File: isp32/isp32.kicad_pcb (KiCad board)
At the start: 2 copper layers, 55.5 x 48.5 mm, 101 parts, among them J1 BAT1, J10 LoRa_ANT, J2 Switching, J3 USB_C_Receptacle_USB2.0, J4 ESP_JTAG, J5 GPS_ANT, J6 F0, J7 F1, J8 Flash_SPI, J9 ANT, M1 Motor_Servo, M2 Motor_Servo, M3 Motor_Servo, M4 Motor_Servo, Q1 BSS138, Q2 BSS138, Q3 IRLML6402, Q4 BSS138, Q5 IRLML6402, Q6 S8050, Q7 S8050, Q8 S8050, SW1 RST, SW2 IO0, U10 BMP280, U11 MPU-9250, U12 CH340C, U2 USBLC6-2SC6, U3 ESP32-WROOM-32U, U4 AMS1117-3.3, U5 MP2303ADN, U7 NEO-XM, U8 AT25SF081-SSHD-X, U9 RFM98W-315S2

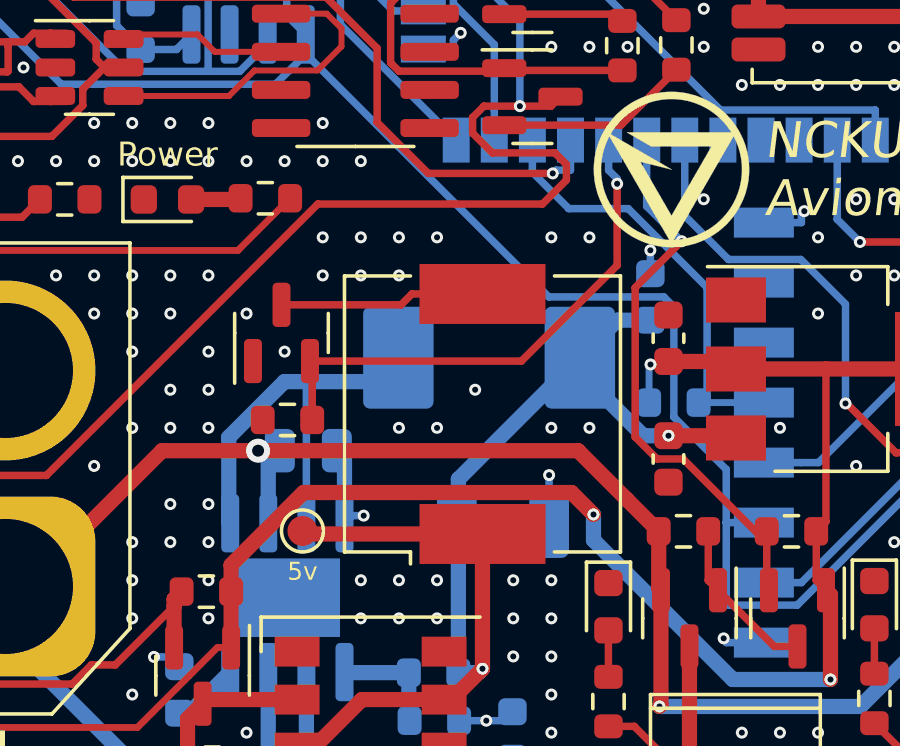
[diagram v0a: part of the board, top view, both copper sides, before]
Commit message: Change buzzer type
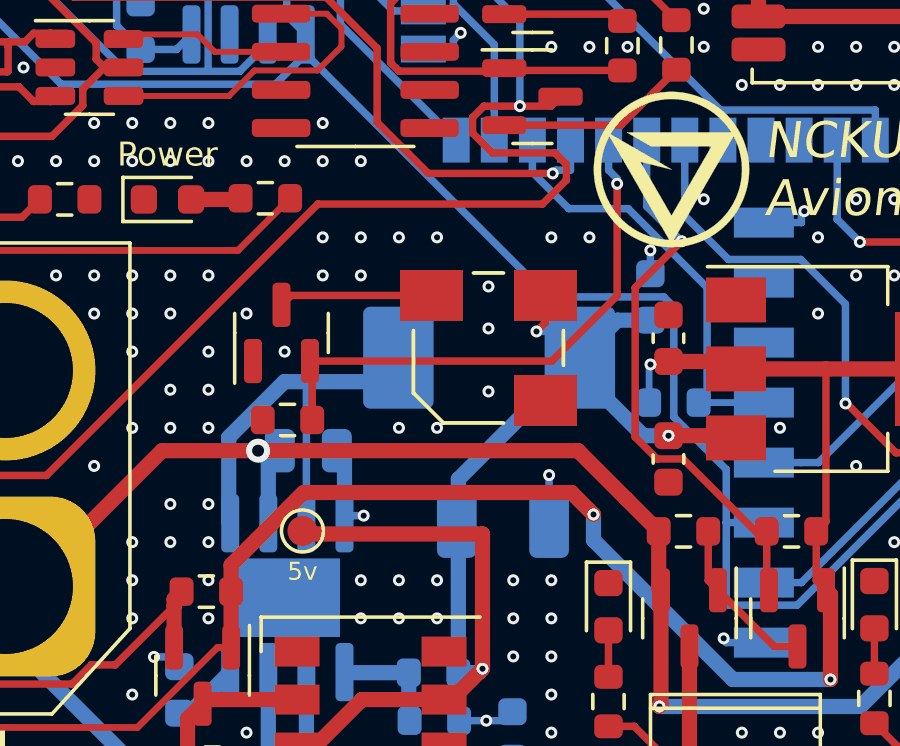
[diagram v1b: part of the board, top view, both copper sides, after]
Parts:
- removed BZ1: Buzzer, Buzzer_Beeper:Buzzer_CUI_CPT-9019S-SMT
- added LS1: 5020, Buzzer:XDCR_KSSG33J12-3, F.Cu at (83.9, 69.5)
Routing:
- net +5V: track 154.7 -> 157.8 mm, vias 6 -> 7
- net Net-(LS1-PadN): track 6.85 -> 5.13 mm
- net Buzz: track 17.8 -> 18.4 mm
- net GND: vias 465 -> 464

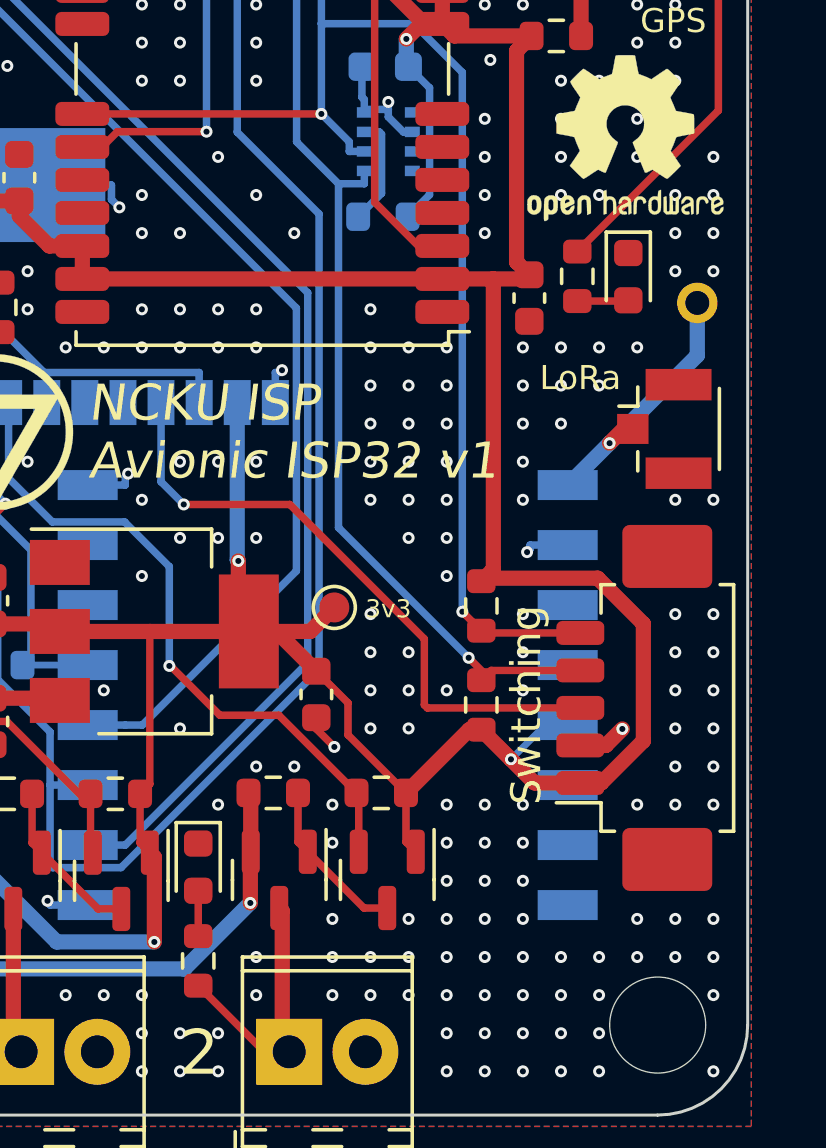
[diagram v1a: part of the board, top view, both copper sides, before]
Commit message: Switching port flip
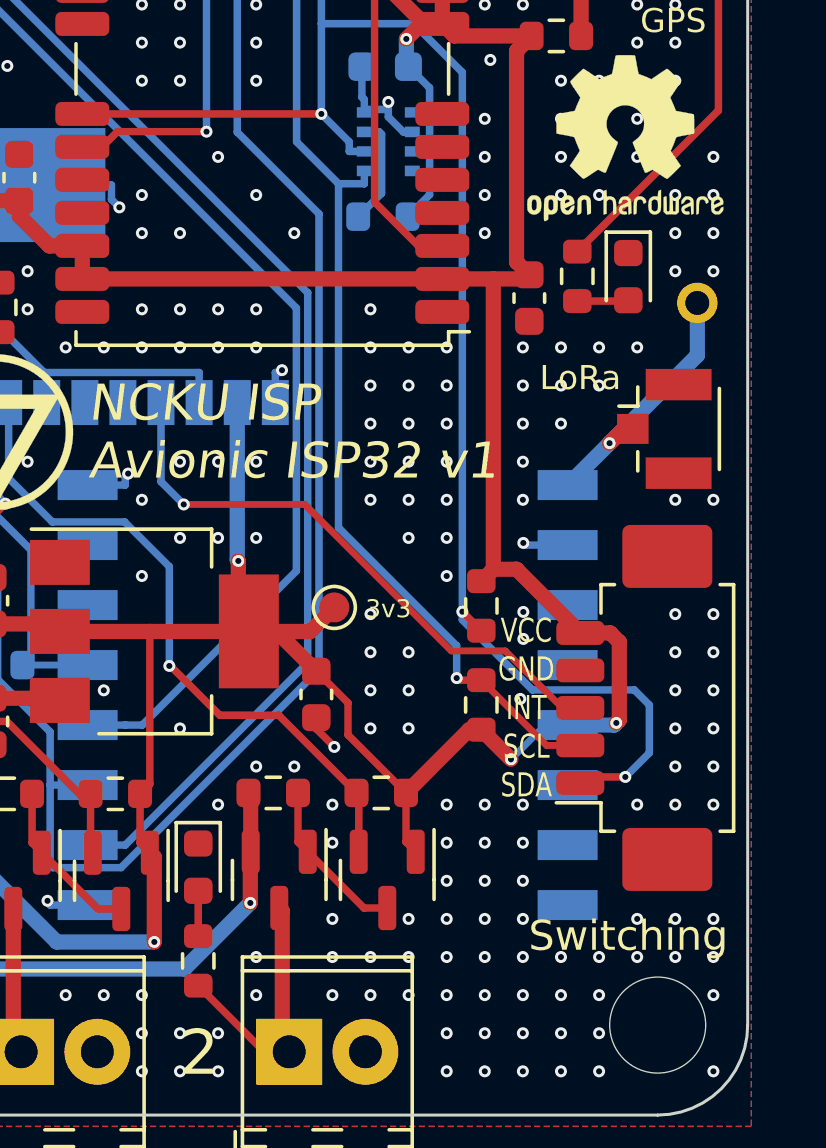
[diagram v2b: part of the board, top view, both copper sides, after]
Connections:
- J2 pad 1: +3V3 -> SDA
- J2 pad 2: GND -> SCL
- J2 pad 4: SCL -> GND
- J2 pad 5: SDA -> +3V3
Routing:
- net SDA: track 56.4 -> 65.0 mm, vias 2 -> 3
- net +3V3: track 260.9 -> 255.4 mm, vias 6 -> 7
- net GND: track 50.1 -> 48.4 mm, vias 464 -> 462
- net SCL: track 52.0 -> 53.3 mm
- net EXT_INT: track 21.0 -> 19.7 mm
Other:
- board text added: "VCC GND INT SCL SDA"

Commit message: Add water mark
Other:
- board text added: "JLCJLCJLCJLC"
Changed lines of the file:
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@@
     (effects (font (size 0.8 0.8) (thickness 0.15)))
   )
-  (gr_text "VCC\nGND\nINT\nSCL\nSDA" (at 107.7 72.7) (layer "F.SilkS")
-    (effects (font (size 0.8 0.6) (thickness 0.1)))
+  (gr_text "VCC\nGND\nINT\nSCL\nSDA" (at 107.7 72.8) (layer "F.SilkS")
+    (effects (font (size 0.8 0.6) (thickness 0.15)))
   )
   (gr_text "LoRa" (at 109.5 61.7) (layer "F.SilkS")
     (effects (font (size 0.8 0.8) (thickness 0.15)))
   )
+  (gr_text "JLCJLCJLCJLC" (at 98.9 52.9 90) (layer "F.SilkS")
+    (effects (font (size 1 1) (thickness 0.15)))
+  )
   (gr_text "3V3 TDI TCK TMS TDO GND" (at 74.1 46.4) (layer "F.SilkS")

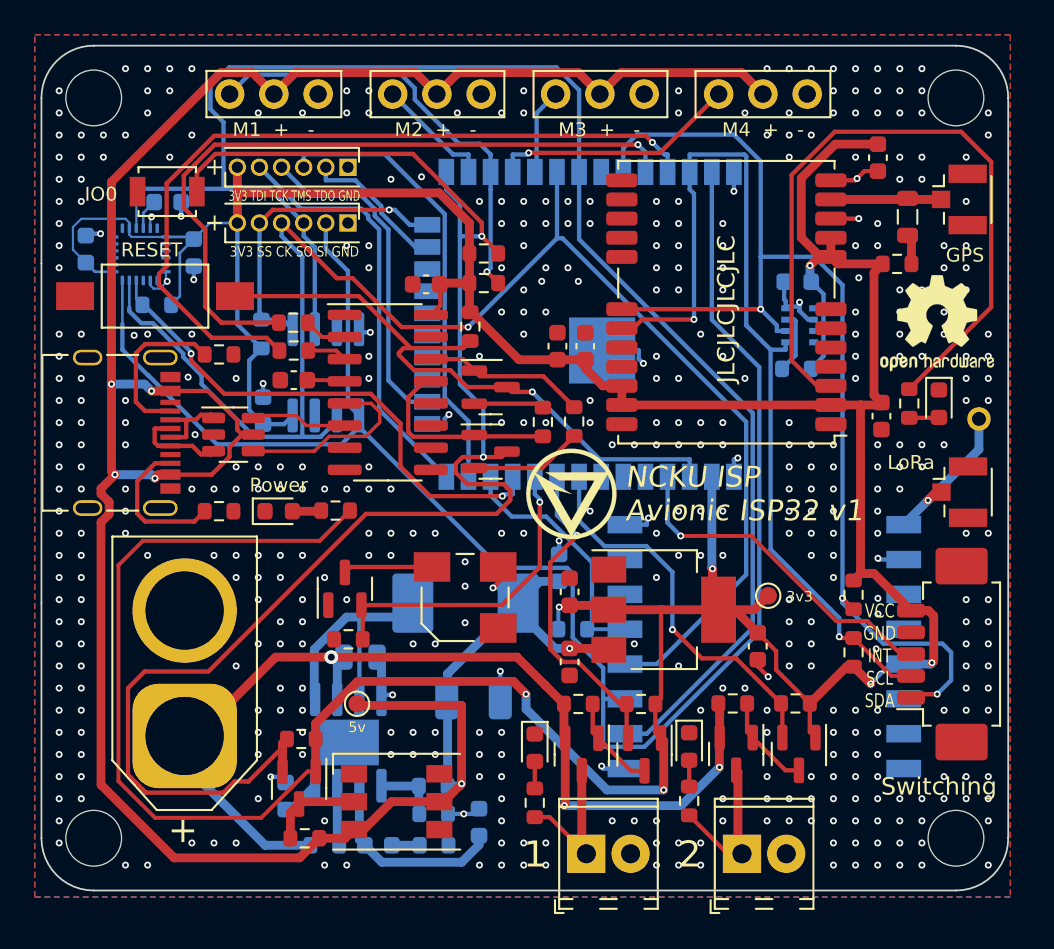
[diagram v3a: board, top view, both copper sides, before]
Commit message: Add sd card and pwm controller
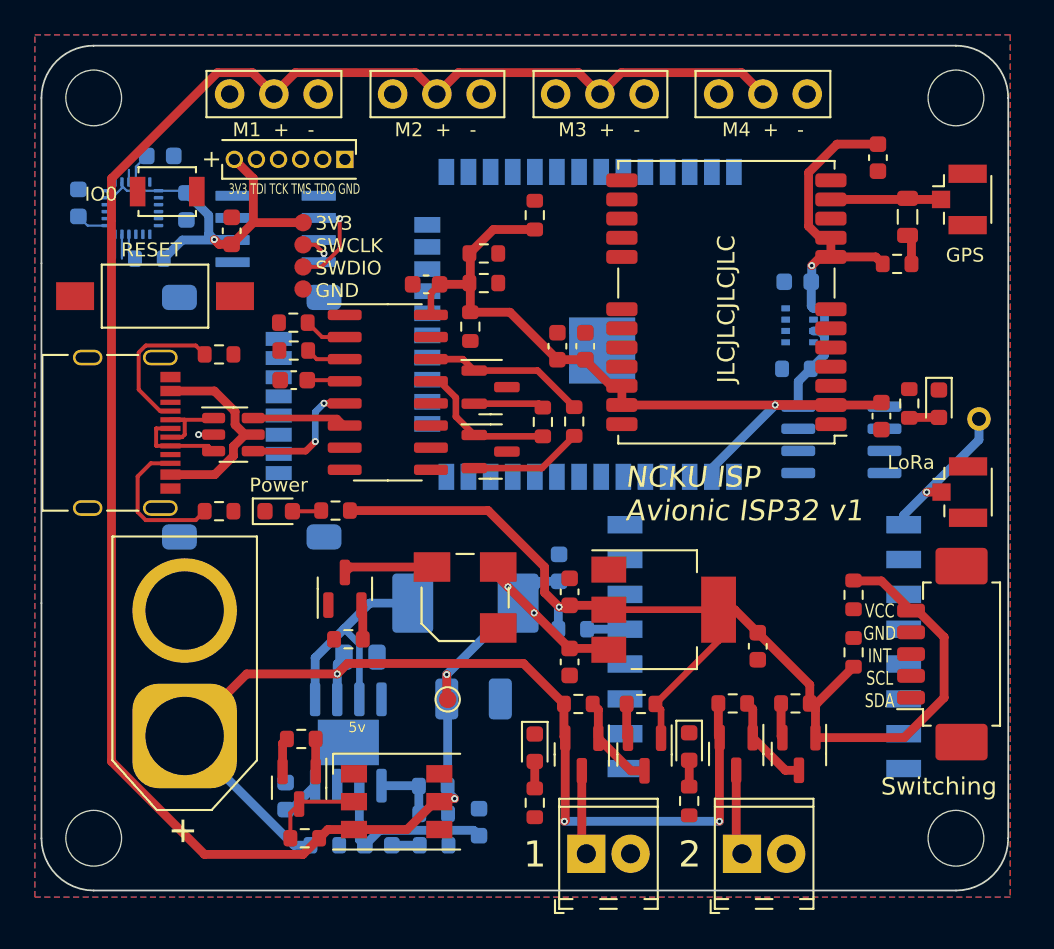
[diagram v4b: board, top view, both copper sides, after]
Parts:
- removed C20: 100n, Capacitor_SMD:C_0603_1608Metric
- removed G***: LOGO, isp_logo:isp_logo
- removed J8: Flash_SPI, Connector_PinHeader_1.27mm:PinHeader_1x06_P1.27mm_Vertical
- removed REF**: OSHW-Logo2_7.3x6mm_SilkScreen, Symbol:OSHW-Logo2_7.3x6mm_SilkScreen
- removed U8: AT25SF081-SSHD-X, Package_SO:SOIC-8_3.9x4.9mm_P1.27mm
- added C3: 100n, Capacitor_SMD:C_0603_1608Metric, F.Cu at (70.5, 48.4)
- added J12: Micro_SD_Card, Connector_Card:microSD_HC_Molex_47219-2001, B.Cu at (71.1, 59.1)
- added TP3: SWDIO, TestPoint:TestPoint_Pad_D1.0mm, F.Cu at (74.6, 50.5)
- added TP4: SWCLK, TestPoint:TestPoint_Pad_D1.0mm, F.Cu at (74.6, 49.2)
- added TP5: GND, TestPoint:TestPoint_Pad_D1.0mm, F.Cu at (74.6, 51.7)
- added U1: STM32G030J6M6, STM32G030J6:SOIC127P600X175-8N, B.Cu at (73.0, 48.3)
- added U6: 24LC32, Package_SO:SOIC-8_3.9x4.9mm_P1.27mm, B.Cu at (105.5, 60.4)
- R30: moved to F.Cu
- TP1: value TP3v3 -> 3V3
- moved TP1 34.2 mm to (74.6, 47.9), turned to 0 degrees
- moved R30 17.1 mm to (87.9, 47.5)
- moved TP2 5.21 mm to (82.9, 75.3)
- moved C23 2.68 mm to (61.7, 46.8)
- moved C22 2.68 mm to (67.9, 47.0)
- moved C24 2.68 mm to (66.4, 44.1)
- moved R17 2.68 mm to (65.8, 50.0)
- moved U11 2.68 mm to (64.8, 47.1)
- moved J4 0.48 mm to (77.0, 44.3)
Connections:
- Q2 pad 2: IO0 -> RGB
- R19 pad 2: IO0 -> RGB
- R30 pad 2: FLASH_SS -> SD_SS
- U11 pad 12: unconnected-(U11-Pad12) -> IMU_INT
- U3 pad 24: FLASH_SS -> RGB
- U3 pad 26: SERVO1 -> LORA_RST
- U3 pad 27: SERVO0 -> TX1
- U3 pad 28: SERVO3 -> RX1
- U3 pad 29: SERVO2 -> SD_SS
- U3 pad 5: unconnected-(U3-Pad5) -> IMU_INT
- U7 pad 18: SDA -> Net-(U6-Pad5)
- U7 pad 19: SCL -> Net-(U6-Pad6)
- U7 pad 20: unconnected-(U7-Pad20) -> RX1
- U7 pad 21: unconnected-(U7-Pad21) -> TX1
- U9 pad 6: unconnected-(U9-Pad6) -> LORA_RST
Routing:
- net MOSI: track 99.6 -> 1.40 mm
- net IO0: track 91.8 -> 0.00 mm, vias 2 -> 0
- net MISO: track 92.2 -> 0.70 mm
- net SCK: track 87.8 -> 1.40 mm, vias 1 -> 0
- net +3V3: track 255.4 -> 169.0 mm, vias 7 -> 4
- net SDA: track 65.0 -> 0.00 mm, vias 3 -> 0
- net SCL: track 53.3 -> 2.03 mm, vias 2 -> 1
- net GND: track 48.4 -> 0.86 mm, vias 462 -> 1
- net RXD: track 45.8 -> 0.00 mm, vias 1 -> 0
- net Net-(R13-Pad1): track 41.7 -> 0.00 mm
- net TXD: track 41.2 -> 0.00 mm, vias 1 -> 0
- net RST: track 36.0 -> 0.00 mm, vias 1 -> 0
- net IMU_SS: track 30.1 -> 1.54 mm, vias 2 -> 0
- net TMS: track 25.9 -> 0.00 mm
- net SERVO0: track 25.5 -> 0.00 mm, vias 1 -> 0
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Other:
- board text added: "3V3 SWCLK SWDIO GND"
- board text removed: "3V3 SS CK SO SI GND"
- board text removed: "3v3"

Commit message: New pcb
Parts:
- added G***: LOGO, isp_logo:isp_logo, F.Cu at (89.3, 63.7)
- added REF**: OSHW-Logo2_7.3x6mm_SilkScreen, Symbol:OSHW-Logo2_7.3x6mm_SilkScreen, F.Cu at (110.0, 54.0)
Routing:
- net SDA: track 0.00 -> 78.6 mm, vias 0 -> 3
- net SCK: track 1.40 -> 79.9 mm, vias 0 -> 4
- net MOSI: track 1.40 -> 79.7 mm, vias 0 -> 3
- net MISO: track 0.70 -> 77.0 mm, vias 0 -> 2
- net SCL: track 2.03 -> 69.7 mm, vias 1 -> 4
- net RXD: track 0.00 -> 60.6 mm, vias 0 -> 3
- net +3V3: track 169.0 -> 221.0 mm, vias 4 -> 7
- net SERVO0: track 0.00 -> 47.0 mm
- net IMU_INT: track 0.00 -> 44.7 mm, vias 0 -> 2
- net SD_SS: track 0.00 -> 43.6 mm, vias 0 -> 3
- net GND: track 0.86 -> 44.3 mm, vias 1 -> 461
- net TCK: track 0.00 -> 43.4 mm, vias 0 -> 4
- net IO0: track 0.00 -> 37.7 mm, vias 0 -> 3
- net RST: track 0.00 -> 33.5 mm, vias 0 -> 2
- net RGB: track 1.97 -> 35.4 mm, vias 0 -> 3
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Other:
- board text removed: "Switching"
